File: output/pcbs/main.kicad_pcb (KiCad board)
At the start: 2 copper layers, 91.2 x 62.6 mm, 19 parts

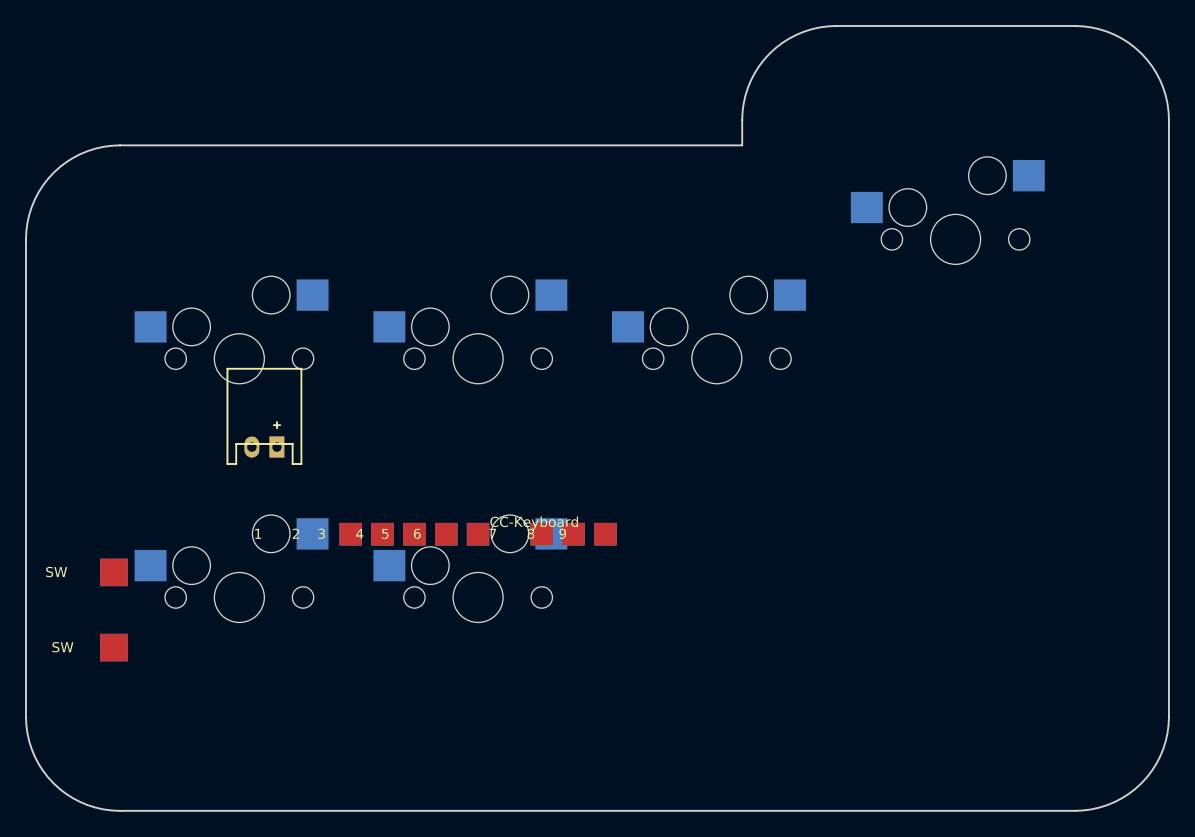
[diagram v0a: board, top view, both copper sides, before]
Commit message: 修复布局与定位板：稀疏列用 skip、行序纠正、plate 补外框、输出 SVG
- 原稀疏写法无效：列内 rows 不能删行，须 skip: true；
  行按声明顺序自 y=0 向上堆叠，bottom 须写在 top 前，
  否则行名与位置颠倒（此前 ESC/←、↑/↓ 键位互换，且多出 2 个孔位）
- plate outline 此前只有轴孔没有板外形，补外框（键阵外扩 edge）+ subtract 挖孔
- ergogen --svg 直接输出 plate.svg/board.svg（填充后处理），
  供 Bambu Studio 等切片软件导入 3D 打印定位板
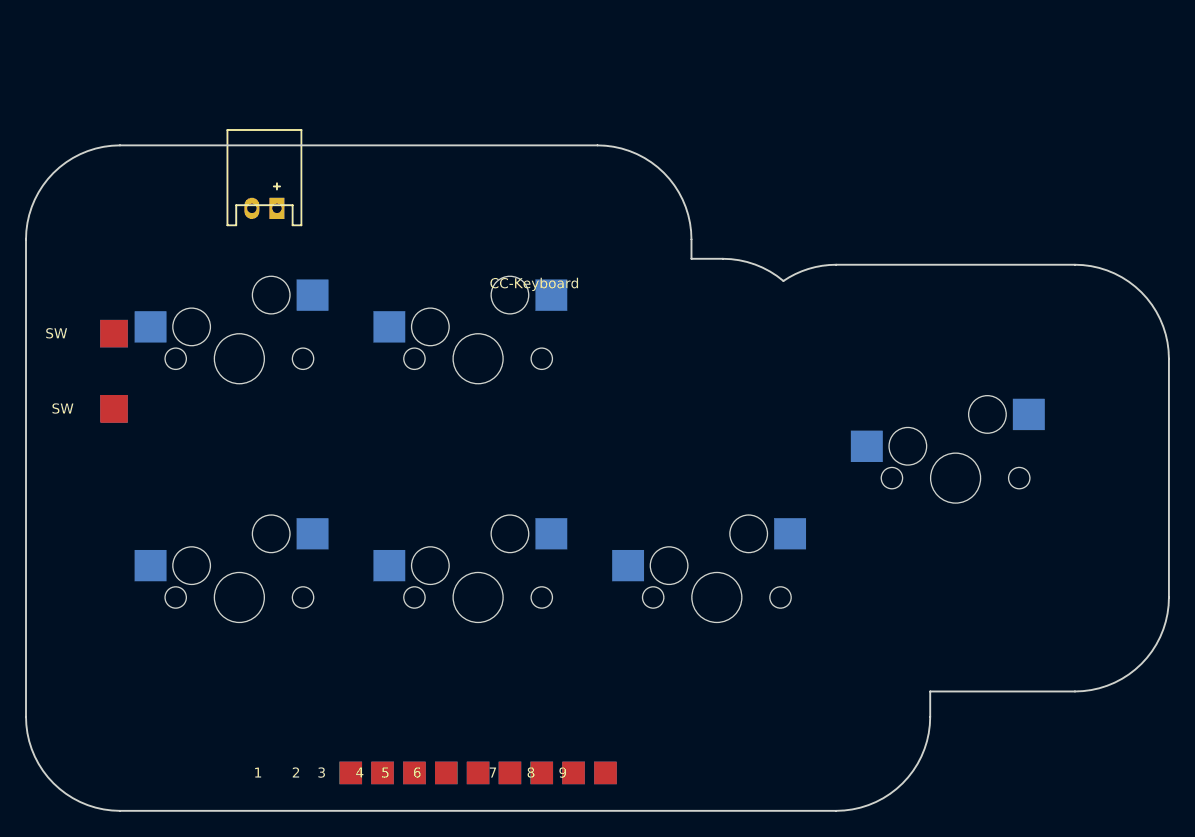
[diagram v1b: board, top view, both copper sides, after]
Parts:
- moved S6 19.1 mm to (57.1, -9.53)
- moved JST1 19.1 mm to (2.00, -31.1)
- moved PAD1 19.1 mm to (8.89, 14.0)
- moved PAD10 19.1 mm to (-10.0, -15.1)
- moved PAD11 19.1 mm to (-10.0, -21.1)
- moved PAD12 19.1 mm to (31.1, -25.1)
- moved PAD2 19.1 mm to (11.4, 14.0)
- moved PAD3 19.1 mm to (14.0, 14.0)
- moved PAD4 19.1 mm to (16.5, 14.0)
- moved PAD5 19.1 mm to (19.1, 14.0)
- moved PAD6 19.1 mm to (21.6, 14.0)
- moved PAD7 19.1 mm to (24.1, 14.0)
- moved PAD8 19.1 mm to (26.7, 14.0)
- moved PAD9 19.1 mm to (29.2, 14.0)
- moved S1 19.1 mm to (0.00, -19.1)
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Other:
- board size 91.2 x 62.6 mm -> 91.2 x 53.1 mm
